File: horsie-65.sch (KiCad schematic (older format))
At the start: 17 parts, among them J1 AVR-ISP-6, J2 Connector_Generic_Conn_01x04, SW68 SW_Push, U2 ATmega32U4-AU, Y1 Crystal_GND24_Small

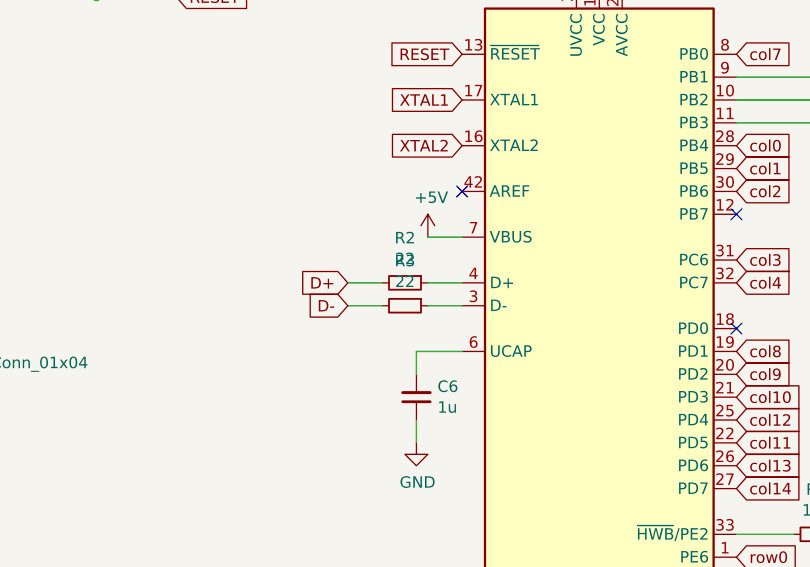
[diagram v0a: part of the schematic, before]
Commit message: flipped switches
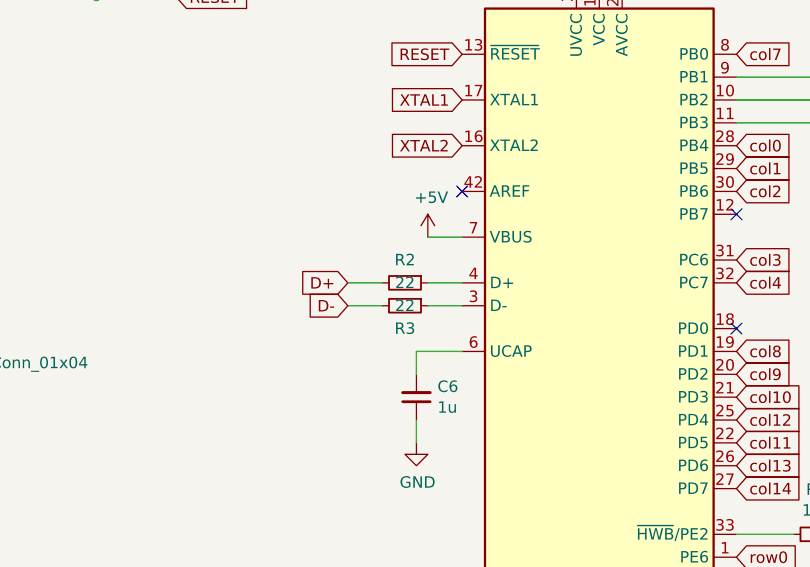
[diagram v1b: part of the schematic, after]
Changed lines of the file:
@@
 EESchema Schematic File Version 4
+LIBS:horsie-65-cache
 EELAYER 30 0
 EELAYER END
@@
 U 1 1 62881754
 P 5450 2850
-F 0 "R2" V 5254 2850 50  0000 C CNN
-F 1 "22" V 5345 2850 50  0000 C CNN
+F 0 "R2" V 5350 2850 50  0000 C CNN
+F 1 "22" V 5450 2850 50  0000 C CNN
 F 2 "Resistor_SMD:R_0805_2012Metric_Pad1.15x1.40mm_HandSolder" H 5450 2850 50  0001 C CNN
 F 3 "~" H 5450 2850 50  0001 C CNN
@@
 U 1 1 62881CC4
 P 5450 2950
-F 0 "R3" V 5254 2950 50  0000 C CNN
-F 1 "22" V 5345 2950 50  0000 C CNN
+F 0 "R3" V 5550 2950 50  0000 C CNN
+F 1 "22" V 5450 2950 50  0000 C CNN
 F 2 "Resistor_SMD:R_0805_2012Metric_Pad1.15x1.40mm_HandSolder" H 5450 2950 50  0001 C CNN
 F 3 "~" H 5450 2950 50  0001 C CNN

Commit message: more pcb
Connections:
- net VCC is gone; now on net +5V: J2.1 (Pin_1)
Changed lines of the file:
@@
 Wire Wire Line
 	3000 1600 3350 1600
+$Comp
+L power:+5V #PWR?
+U 1 1 63005D74
+P 3150 2600
+F 0 "#PWR?" H 3150 2450 50  0001 C CNN
+F 1 "+5V" H 3165 2773 50  0000 C CNN
+F 2 "" H 3150 2600 50  0001 C CNN
+F 3 "" H 3150 2600 50  0001 C CNN
+	1    3150 2600
+	1    0    0    -1
+$EndComp
+Wire Wire Line
+	3150 2600 3350 2600
+Connection ~ 3350 2600
 $EndSCHEMATC

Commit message: more routing
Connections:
- net row0: now also U2.39 (PF4); no longer U2.1 (PE6)
- net row1: now also U2.40 (PF1); no longer U2.38 (PF5)
- net row3: now also U2.1 (PE6); no longer U2.40 (PF1)
- net row4: now also U2.38 (PF5); no longer U2.39 (PF4)
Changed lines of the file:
@@
 Text GLabel 6900 3750 2    50   Input ~ 0
 col14
-Text GLabel 6900 4050 2    50   Input ~ 0
+Text GLabel 6900 4450 2    50   Input ~ 0
 row0
 Text GLabel 6900 4250 2    50   Input ~ 0
 row2
+Text GLabel 6900 4050 2    50   Input ~ 0
+row3
+Text GLabel 6900 4550 2    50   Input ~ 0
+row4
 Text GLabel 6900 4350 2    50   Input ~ 0
-row3
-Text GLabel 6900 4450 2    50   Input ~ 0
-row4
-Text GLabel 6900 4550 2    50   Input ~ 0
 row1
 Text GLabel 6900 4650 2    50   Input ~ 0
@@
 	3000 1600 3350 1600
 $Comp
-L power:+5V #PWR?
+L power:+5V #PWR0101
 U 1 1 63005D74
 P 3150 2600
-F 0 "#PWR?" H 3150 2450 50  0001 C CNN
+F 0 "#PWR0101" H 3150 2450 50  0001 C CNN
 F 1 "+5V" H 3165 2773 50  0000 C CNN
 F 2 "" H 3150 2600 50  0001 C CNN

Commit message: aesthetics 1
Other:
- moved on the sheet: C6, R2, R3, R4, U2
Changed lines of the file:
@@
 L MCU_Microchip_ATmega:ATmega32U4-AU U2
 U 1 1 6283C2E5
-P 6300 3350
-F 0 "U2" H 6300 1461 50  0000 C CNN
-F 1 "ATmega32U4-AU" H 6300 1370 50  0000 C CNN
-F 2 "Package_QFP:TQFP-44_10x10mm_P0.8mm" H 6300 3350 50  0001 C CIN
-F 3 "http://ww1.microchip.com/downloads/en/DeviceDoc/Atmel-7766-8-bit-AVR-ATmega16U4-32U4_Datasheet.pdf" H 6300 3350 50  0001 C CNN
-	1    6300 3350
+P 6000 2700
+F 0 "U2" H 6000 811 50  0000 C CNN
+F 1 "ATmega32U4-AU" H 6000 720 50  0000 C CNN
+F 2 "Package_QFP:TQFP-44_10x10mm_P0.8mm" H 6000 2700 50  0001 C CIN
+F 3 "http://ww1.microchip.com/downloads/en/DeviceDoc/Atmel-7766-8-bit-AVR-ATmega16U4-32U4_Datasheet.pdf" H 6000 2700 50  0001 C CNN
+	1    6000 2700
 	1    0    0    -1
 $EndComp
@@
 L power:+5V #PWR03
 U 1 1 6283F3B3
-P 6200 1450
-F 0 "#PWR03" H 6200 1300 50  0001 C CNN
-F 1 "+5V" H 6215 1623 50  0000 C CNN
-F 2 "" H 6200 1450 50  0001 C CNN
-F 3 "" H 6200 1450 50  0001 C CNN
-	1    6200 1450
-	1    0    0    -1
-$EndComp
-Wire Wire Line
-	6200 1450 6200 1550
-Wire Wire Line
-	6200 1550 6300 1550
-Connection ~ 6200 1550
-Wire Wire Line
-	6300 1550 6400 1550
-Connection ~ 6300 1550
-Wire Wire Line
-	6300 5150 6200 5150
+P 5900 800
+F 0 "#PWR03" H 5900 650 50  0001 C CNN
+F 1 "+5V" H 5915 973 50  0000 C CNN
+F 2 "" H 5900 800 50  0001 C CNN
+F 3 "" H 5900 800 50  0001 C CNN
+	1    5900 800
+	1    0    0    -1
+$EndComp
+Wire Wire Line
+	5900 800  5900 900
+Wire Wire Line
+	5900 900  6000 900
+Connection ~ 5900 900
+Wire Wire Line
+	6000 900  6100 900
+Connection ~ 6000 900
+Wire Wire Line
+	6000 4500 5900 4500
 $Comp
 L power:GND #PWR014
 U 1 1 6284044C
-P 6200 5250
-F 0 "#PWR014" H 6200 5000 50  0001 C CNN
-F 1 "GND" H 6205 5077 50  0000 C CNN
-F 2 "" H 6200 5250 50  0001 C CNN
-F 3 "" H 6200 5250 50  0001 C CNN
-	1    6200 5250
-	1    0    0    -1
-$EndComp
-Wire Wire Line
-	6200 5150 6200 5250
-Connection ~ 6200 5150
-Text GLabel 5700 2050 0    50   Input ~ 0
+P 5900 4600
+F 0 "#PWR014" H 5900 4350 50  0001 C CNN
+F 1 "GND" H 5905 4427 50  0000 C CNN
+F 2 "" H 5900 4600 50  0001 C CNN
+F 3 "" H 5900 4600 50  0001 C CNN
+	1    5900 4600
+	1    0    0    -1
+$EndComp
+Wire Wire Line
+	5900 4500 5900 4600
+Connection ~ 5900 4500
+Text GLabel 5400 1400 0    50   Input ~ 0
 XTAL1
-Text GLabel 5700 2250 0    50   Input ~ 0
+Text GLabel 5400 1600 0    50   Input ~ 0
 XTAL2
-Text GLabel 5200 2850 0    50   Input ~ 0
+Text GLabel 4900 2200 0    50   Input ~ 0
 D+
-Text GLabel 5200 2950 0    50   Input ~ 0
+Text GLabel 4900 2300 0    50   Input ~ 0
 D-
 $Comp
 L Device:R_Small R4
 U 1 1 62841E9C
-P 7250 3950
-F 0 "R4" V 7054 3950 50  0000 C CNN
-F 1 "10k" V 7145 3950 50  0000 C CNN
-F 2 "Resistor_SMD:R_0805_2012Metric_Pad1.15x1.40mm_HandSolder" H 7250 3950 50  0001 C CNN
-F 3 "~" H 7250 3950 50  0001 C CNN
-	1    7250 3950
+P 6950 3300
+F 0 "R4" V 6754 3300 50  0000 C CNN
+F 1 "10k" V 6845 3300 50  0000 C CNN
+F 2 "Resistor_SMD:R_0805_2012Metric_Pad1.15x1.40mm_HandSolder" H 6950 3300 50  0001 C CNN
+F 3 "~" H 6950 3300 50  0001 C CNN
+	1    6950 3300
 	0    1    1    0
 $EndComp
 Wire Wire Line
-	6900 3950 7150 3950
+	6600 3300 6850 3300
 $Comp
 L power:GND #PWR012
 U 1 1 62843533
-P 7550 3950
-F 0 "#PWR012" H 7550 3700 50  0001 C CNN
-F 1 "GND" H 7555 3777 50  0000 C CNN
-F 2 "" H 7550 3950 50  0001 C CNN
-F 3 "" H 7550 3950 50  0001 C CNN
-	1    7550 3950
-	1    0    0    -1
-$EndComp
-Wire Wire Line
-	7550 3950 7350 3950
-NoConn ~ 5700 2450
+P 7250 3300
+F 0 "#PWR012" H 7250 3050 50  0001 C CNN
+F 1 "GND" H 7255 3127 50  0000 C CNN
+F 2 "" H 7250 3300 50  0001 C CNN
+F 3 "" H 7250 3300 50  0001 C CNN
+	1    7250 3300
+	1    0    0    -1
+$EndComp
+Wire Wire Line
+	7250 3300 7050 3300
+NoConn ~ 5400 1800
 $Comp
 L power:+5V #PWR08
 U 1 1 62844DBF
-P 5550 2650
-F 0 "#PWR08" H 5550 2500 50  0001 C CNN
-F 1 "+5V" H 5565 2823 50  0000 C CNN
-F 2 "" H 5550 2650 50  0001 C CNN
-F 3 "" H 5550 2650 50  0001 C CNN
-	1    5550 2650
-	1    0    0    -1
-$EndComp
-Wire Wire Line
-	5550 2650 5700 2650
-Text GLabel 5700 1850 0    50   Input ~ 0
+P 5250 2000
+F 0 "#PWR08" H 5250 1850 50  0001 C CNN
+F 1 "+5V" H 5265 2173 50  0000 C CNN
+F 2 "" H 5250 2000 50  0001 C CNN
+F 3 "" H 5250 2000 50  0001 C CNN
+	1    5250 2000
+	1    0    0    -1
+$EndComp
+Wire Wire Line
+	5250 2000 5400 2000
+Text GLabel 5400 1200 0    50   Input ~ 0
 RESET
-Text GLabel 7250 1950 2    50   Input ~ 0
+Text GLabel 6950 1300 2    50   Input ~ 0
 SCK
-Text GLabel 7250 2050 2    50   Input ~ 0
+Text GLabel 6950 1400 2    50   Input ~ 0
 MOSI
-Text GLabel 7250 2150 2    50   Input ~ 0
+Text GLabel 6950 1500 2    50   Input ~ 0
 MISO
 Wire Wire Line
-	7250 2050 6900 2050
-Wire Wire Line
-	6900 1950 7250 1950
+	6950 1400 6600 1400
+Wire Wire Line
+	6600 1300 6950 1300
 $Comp
 L Device:C_Small C6
 U 1 1 62846732
-P 5500 3350
-F 0 "C6" H 5408 3304 50  0000 R CNN
-F 1 "1u" H 5408 3395 50  0000 R CNN
-F 2 "Capacitor_SMD:C_0805_2012Metric_Pad1.15x1.40mm_HandSolder" H 5500 3350 50  0001 C CNN
-F 3 "~" H 5500 3350 50  0001 C CNN
-	1    5500 3350
+P 5200 2700
+F 0 "C6" H 5108 2654 50  0000 R CNN
+F 1 "1u" H 5108 2745 50  0000 R CNN
+F 2 "Capacitor_SMD:C_0805_2012Metric_Pad1.15x1.40mm_HandSolder" H 5200 2700 50  0001 C CNN
+F 3 "~" H 5200 2700 50  0001 C CNN
+	1    5200 2700
 	-1   0    0    1
 $EndComp
 Wire Wire Line
-	5700 3150 5500 3150
-Wire Wire Line
-	5500 3150 5500 3250
+	5400 2500 5200 2500
+Wire Wire Line
+	5200 2500 5200 2600
 $Comp
 L power:GND #PWR011
 U 1 1 62847E4C
-P 5500 3550
-F 0 "#PWR011" H 5500 3300 50  0001 C CNN
-F 1 "GND" H 5505 3377 50  0000 C CNN
-F 2 "" H 5500 3550 50  0001 C CNN
-F 3 "" H 5500 3550 50  0001 C CNN
-	1    5500 3550
-	1    0    0    -1
-$EndComp
-Wire Wire Line
-	5500 3550 5500 3450
-Wire Wire Line
-	6900 2150 7250 2150
+P 5200 2900
+F 0 "#PWR011" H 5200 2650 50  0001 C CNN
+F 1 "GND" H 5205 2727 50  0000 C CNN
+F 2 "" H 5200 2900 50  0001 C CNN
+F 3 "" H 5200 2900 50  0001 C CNN
+	1    5200 2900
+	1    0    0    -1
+$EndComp
+Wire Wire Line
+	5200 2900 5200 2800
+Wire Wire Line
+	6600 1500 6950 1500
 Text GLabel 4450 1600 2    50   Input ~ 0
 RESET
@@
 L Device:R_Small R2
 U 1 1 62881754
-P 5450 2850
-F 0 "R2" V 5350 2850 50  0000 C CNN
-F 1 "22" V 5450 2850 50  0000 C CNN
-F 2 "Resistor_SMD:R_0805_2012Metric_Pad1.15x1.40mm_HandSolder" H 5450 2850 50  0001 C CNN
-F 3 "~" H 5450 2850 50  0001 C CNN
-	1    5450 2850
+P 5150 2200
+F 0 "R2" V 5050 2200 50  0000 C CNN
+F 1 "22" V 5150 2200 50  0000 C CNN
+F 2 "Resistor_SMD:R_0805_2012Metric_Pad1.15x1.40mm_HandSolder" H 5150 2200 50  0001 C CNN
+F 3 "~" H 5150 2200 50  0001 C CNN
+	1    5150 2200
 	0    1    1    0
 $EndComp
@@
 L Device:R_Small R3
 U 1 1 62881CC4
-P 5450 2950
-F 0 "R3" V 5550 2950 50  0000 C CNN
-F 1 "22" V 5450 2950 50  0000 C CNN
-F 2 "Resistor_SMD:R_0805_2012Metric_Pad1.15x1.40mm_HandSolder" H 5450 2950 50  0001 C CNN
-F 3 "~" H 5450 2950 50  0001 C CNN
-	1    5450 2950
+P 5150 2300
+F 0 "R3" V 5250 2300 50  0000 C CNN
+F 1 "22" V 5150 2300 50  0000 C CNN
+F 2 "Resistor_SMD:R_0805_2012Metric_Pad1.15x1.40mm_HandSolder" H 5150 2300 50  0001 C CNN
+F 3 "~" H 5150 2300 50  0001 C CNN
+	1    5150 2300
 	0    1    1    0
 $EndComp
 Wire Wire Line
-	5350 2850 5200 2850
-Wire Wire Line
-	5200 2950 5350 2950
-Wire Wire Line
-	5550 2950 5700 2950
-Wire Wire Line
-	5700 2850 5550 2850
+	5050 2200 4900 2200
+Wire Wire Line
+	4900 2300 5050 2300
+Wire Wire Line
+	5250 2300 5400 2300
+Wire Wire Line
+	5400 2200 5250 2200
 $Comp
 L Connector:AVR-ISP-6 J1
@@
 Wire Wire Line
 	1750 3850 1750 4000
-$Sheet
-S 750  4450 4750 3250
-U 628A0341
-F0 "matrix" 50
-F1 "matrix.sch" 50
-$EndSheet
-Text GLabel 6900 1850 2    50   Input ~ 0
+Text GLabel 6600 1200 2    50   Input ~ 0
 col7
-Text GLabel 6900 2250 2    50   Input ~ 0
+Text GLabel 6600 1600 2    50   Input ~ 0
 col0
-Text GLabel 6900 2350 2    50   Input ~ 0
+Text GLabel 6600 1700 2    50   Input ~ 0
 col1
-Text GLabel 6900 2450 2    50   Input ~ 0
+Text GLabel 6600 1800 2    50   Input ~ 0
 col2
-NoConn ~ 6900 2550
-Text GLabel 6900 2750 2    50   Input ~ 0
+NoConn ~ 6600 1900
+Text GLabel 6600 2100 2    50   Input ~ 0
 col3
-Text GLabel 6900 2850 2    50   Input ~ 0
+Text GLabel 6600 2200 2    50   Input ~ 0
 col4
-NoConn ~ 6900 3050
-Text GLabel 6900 3150 2    50   Input ~ 0
+NoConn ~ 6600 2400
+Text GLabel 6600 2500 2    50   Input ~ 0
 col8
-Text GLabel 6900 3250 2    50   Input ~ 0
+Text GLabel 6600 2600 2    50   Input ~ 0
 col9
-Text GLabel 6900 3350 2    50   Input ~ 0
+Text GLabel 6600 2700 2    50   Input ~ 0
 col10
-Text GLabel 6900 3450 2    50   Input ~ 0
+Text GLabel 6600 2800 2    50   Input ~ 0
 col12
-Text GLabel 6900 3550 2    50   Input ~ 0
+Text GLabel 6600 2900 2    50   Input ~ 0
 col11
-Text GLabel 6900 3650 2    50   Input ~ 0
+Text GLabel 6600 3000 2    50   Input ~ 0
 col13
-Text GLabel 6900 3750 2    50   Input ~ 0
+Text GLabel 6600 3100 2    50   Input ~ 0
 col14
-Text GLabel 6900 4450 2    50   Input ~ 0
+Text GLabel 6600 3800 2    50   Input ~ 0
 row0
-Text GLabel 6900 4250 2    50   Input ~ 0
+Text GLabel 6600 3600 2    50   Input ~ 0
 row2
-Text GLabel 6900 4050 2    50   Input ~ 0
+Text GLabel 6600 3400 2    50   Input ~ 0
 row3
-Text GLabel 6900 4550 2    50   Input ~ 0
+Text GLabel 6600 3900 2    50   Input ~ 0
 row4
-Text GLabel 6900 4350 2    50   Input ~ 0
+Text GLabel 6600 3700 2    50   Input ~ 0
 row1
-Text GLabel 6900 4650 2    50   Input ~ 0
+Text GLabel 6600 4000 2    50   Input ~ 0
 col5
-Text GLabel 6900 4750 2    50   Input ~ 0
+Text GLabel 6600 4100 2    50   Input ~ 0
 col6
 $Comp
@@
 	3150 2600 3350 2600
 Connection ~ 3350 2600
+$Sheet
+S 650  4350 4750 3250
+U 628A0341
+F0 "matrix" 50
+F1 "matrix.sch" 50
+$EndSheet
 $EndSCHEMATC
